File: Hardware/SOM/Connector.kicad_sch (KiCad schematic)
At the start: 1 part, among them J1 SODIMM-200_Split

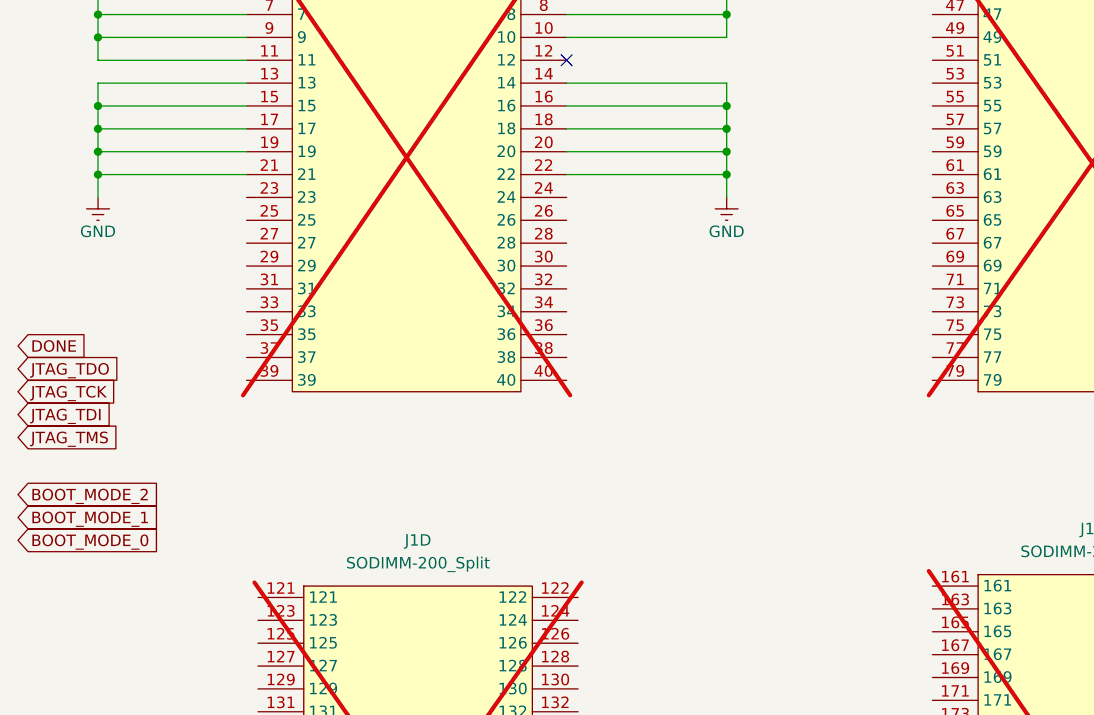
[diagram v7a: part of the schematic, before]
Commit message: SOM: layout update (QSPI+
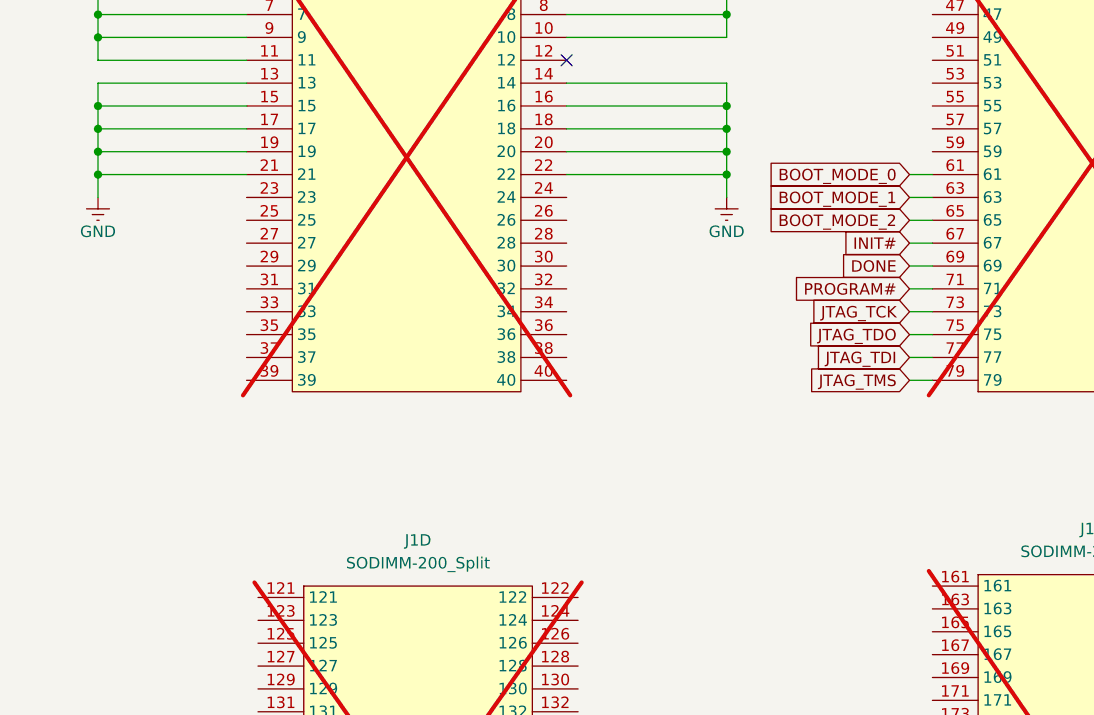
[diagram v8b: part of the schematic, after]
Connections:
- net BOOT_MODE_0: now also J1.61
- net BOOT_MODE_1: now also J1.63
- net BOOT_MODE_2: now also J1.65
- net DONE: now also J1.69
- net JTAG_TCK: now also J1.73
- net JTAG_TDI: now also J1.77
- net JTAG_TDO: now also J1.75
- net JTAG_TMS: now also J1.79
- net INIT#: now reaches J1.67
- net PROGRAM#: now reaches J1.71
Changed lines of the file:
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@@
+	(wire
+		(pts
+			(xy 119.38 68.58) (xy 121.92 68.58)
+		)
+		(stroke
+			(width 0)
+			(type default)
+		)
+	)
 	(wire
 		(pts
@@
 	(wire
 		(pts
+			(xy 119.38 78.74) (xy 121.92 78.74)
+		)
+		(stroke
+			(width 0)
+			(type default)
+		)
+	)
+	(wire
+		(pts
 			(xy 99.06 35.56) (xy 99.06 33.02)
 		)
@@
 	(wire
 		(pts
+			(xy 119.38 66.04) (xy 121.92 66.04)
+		)
+		(stroke
+			(width 0)
+			(type default)
+		)
+	)
+	(wire
+		(pts
 			(xy 99.06 50.8) (xy 99.06 53.34)
 		)
@@
 	(wire
 		(pts
+			(xy 119.38 63.5) (xy 121.92 63.5)
+		)
+		(stroke
+			(width 0)
+			(type default)
+		)
+	)
+	(wire
+		(pts
 			(xy 99.06 33.02) (xy 99.06 30.48)
 		)
@@
 	(wire
 		(pts
+			(xy 119.38 60.96) (xy 121.92 60.96)
+		)
+		(stroke
+			(width 0)
+			(type default)
+		)
+	)
+	(wire
+		(pts
 			(xy 99.06 38.1) (xy 99.06 35.56)
 		)
@@
 	(wire
 		(pts
+			(xy 119.38 73.66) (xy 121.92 73.66)
+		)
+		(stroke
+			(width 0)
+			(type default)
+		)
+	)
+	(wire
+		(pts
+			(xy 119.38 71.12) (xy 121.92 71.12)
+		)
+		(stroke
+			(width 0)
+			(type default)
+		)
+	)
+	(wire
+		(pts
 			(xy 29.21 40.64) (xy 29.21 38.1)
 		)
@@
 	(wire
 		(pts
+			(xy 119.38 76.2) (xy 121.92 76.2)
+		)
+		(stroke
+			(width 0)
+			(type default)
+		)
+	)
+	(wire
+		(pts
 			(xy 81.28 38.1) (xy 99.06 38.1)
 		)
@@
 	(wire
 		(pts
+			(xy 119.38 55.88) (xy 121.92 55.88)
+		)
+		(stroke
+			(width 0)
+			(type default)
+		)
+	)
+	(wire
+		(pts
 			(xy 29.21 48.26) (xy 45.72 48.26)
 		)
@@
 	(wire
 		(pts
+			(xy 119.38 58.42) (xy 121.92 58.42)
+		)
+		(stroke
+			(width 0)
+			(type default)
+		)
+	)
+	(wire
+		(pts
 			(xy 99.06 45.72) (xy 99.06 48.26)
 		)
@@
 	(global_label "JTAG_TDI"
 		(shape input)
-		(at 20.32 82.55 0)
-		(fields_autoplaced yes)
-		(effects
-			(font
-				(size 1.27 1.27)
-			)
-			(justify left)
-		)
-		(property "Intersheetrefs" "${INTERSHEET_REFS}"
-			(at 31.409 82.55 0)
-			(effects
-				(font
-					(size 1.27 1.27)
-				)
-				(justify left)
+		(at 119.38 76.2 180)
+		(fields_autoplaced yes)
+		(effects
+			(font
+				(size 1.27 1.27)
+			)
+			(justify right)
+		)
+		(property "Intersheetrefs" "${INTERSHEET_REFS}"
+			(at 108.291 76.2 0)
+			(effects
+				(font
+					(size 1.27 1.27)
+				)
+				(justify right)
+				(hide yes)
+			)
+		)
+	)
+	(global_label "PROGRAM#"
+		(shape input)
+		(at 119.38 68.58 180)
+		(fields_autoplaced yes)
+		(effects
+			(font
+				(size 1.27 1.27)
+			)
+			(justify right)
+		)
+		(property "Intersheetrefs" "${INTERSHEET_REFS}"
+			(at 106.1743 68.58 0)
+			(effects
+				(font
+					(size 1.27 1.27)
+				)
+				(justify right)
 				(hide yes)
 			)
@@
 	(global_label "BOOT_MODE_2"
 		(shape input)
-		(at 20.32 91.44 0)
-		(fields_autoplaced yes)
-		(effects
-			(font
-				(size 1.27 1.27)
-			)
-			(justify left)
-		)
-		(property "Intersheetrefs" "${INTERSHEET_REFS}"
-			(at 36.5494 91.44 0)
-			(effects
-				(font
-					(size 1.27 1.27)
-				)
-				(justify left)
+		(at 119.38 60.96 180)
+		(fields_autoplaced yes)
+		(effects
+			(font
+				(size 1.27 1.27)
+			)
+			(justify right)
+		)
+		(property "Intersheetrefs" "${INTERSHEET_REFS}"
+			(at 103.1506 60.96 0)
+			(effects
+				(font
+					(size 1.27 1.27)
+				)
+				(justify right)
 				(hide yes)
 			)
@@
 	(global_label "JTAG_TCK"
 		(shape input)
-		(at 20.32 80.01 0)
-		(fields_autoplaced yes)
-		(effects
-			(font
-				(size 1.27 1.27)
-			)
-			(justify left)
-		)
-		(property "Intersheetrefs" "${INTERSHEET_REFS}"
-			(at 32.0742 80.01 0)
-			(effects
-				(font
-					(size 1.27 1.27)
-				)
-				(justify left)
+		(at 119.38 71.12 180)
+		(fields_autoplaced yes)
+		(effects
+			(font
+				(size 1.27 1.27)
+			)
+			(justify right)
+		)
+		(property "Intersheetrefs" "${INTERSHEET_REFS}"
+			(at 107.6258 71.12 0)
+			(effects
+				(font
+					(size 1.27 1.27)
+				)
+				(justify right)
 				(hide yes)
 			)
@@
 	(global_label "BOOT_MODE_1"
 		(shape input)
-		(at 20.32 93.98 0)
-		(fields_autoplaced yes)
-		(effects
-			(font
-				(size 1.27 1.27)
-			)
-			(justify left)
-		)
-		(property "Intersheetrefs" "${INTERSHEET_REFS}"
-			(at 36.5494 93.98 0)
-			(effects
-				(font
-					(size 1.27 1.27)
-				)
-				(justify left)
+		(at 119.38 58.42 180)
+		(fields_autoplaced yes)
+		(effects
+			(font
+				(size 1.27 1.27)
+			)
+			(justify right)
+		)
+		(property "Intersheetrefs" "${INTERSHEET_REFS}"
+			(at 103.1506 58.42 0)
+			(effects
+				(font
+					(size 1.27 1.27)
+				)
+				(justify right)
 				(hide yes)
 			)
@@
 	(global_label "JTAG_TDO"
 		(shape input)
-		(at 20.32 77.47 0)
-		(fields_autoplaced yes)
-		(effects
-			(font
-				(size 1.27 1.27)
-			)
-			(justify left)
-		)
-		(property "Intersheetrefs" "${INTERSHEET_REFS}"
-			(at 32.1347 77.47 0)
-			(effects
-				(font
-					(size 1.27 1.27)
-				)
-				(justify left)
+		(at 119.38 73.66 180)
+		(fields_autoplaced yes)
+		(effects
+			(font
+				(size 1.27 1.27)
+			)
+			(justify right)
+		)
+		(property "Intersheetrefs" "${INTERSHEET_REFS}"
+			(at 107.5653 73.66 0)
+			(effects
+				(font
+					(size 1.27 1.27)
+				)
+				(justify right)
+				(hide yes)
+			)
+		)
+	)
+	(global_label "INIT#"
+		(shape input)
+		(at 119.38 63.5 180)
+		(fields_autoplaced yes)
+		(effects
+			(font
+				(size 1.27 1.27)
+			)
+			(justify right)
+		)
+		(property "Intersheetrefs" "${INTERSHEET_REFS}"
+			(at 111.6171 63.5 0)
+			(effects
+				(font
+					(size 1.27 1.27)
+				)
+				(justify right)
 				(hide yes)
 			)
@@
 	(global_label "BOOT_MODE_0"
 		(shape input)
-		(at 20.32 96.52 0)
-		(fields_autoplaced yes)
-		(effects
-			(font
-				(size 1.27 1.27)
-			)
-			(justify left)
-		)
-		(property "Intersheetrefs" "${INTERSHEET_REFS}"
-			(at 36.5494 96.52 0)
-			(effects
-				(font
-					(size 1.27 1.27)
-				)
-				(justify left)
+		(at 119.38 55.88 180)
+		(fields_autoplaced yes)
+		(effects
+			(font
+				(size 1.27 1.27)
+			)
+			(justify right)
+		)
+		(property "Intersheetrefs" "${INTERSHEET_REFS}"
+			(at 103.1506 55.88 0)
+			(effects
+				(font
+					(size 1.27 1.27)
+				)
+				(justify right)
 				(hide yes)
 			)
@@
 	(global_label "DONE"
 		(shape input)
-		(at 20.32 74.93 0)
-		(fields_autoplaced yes)
-		(effects
-			(font
-				(size 1.27 1.27)
-			)
-			(justify left)
-		)
-		(property "Intersheetrefs" "${INTERSHEET_REFS}"
-			(at 28.3852 74.93 0)
-			(effects
-				(font
-					(size 1.27 1.27)
-				)
-				(justify left)
+		(at 119.38 66.04 180)
+		(fields_autoplaced yes)
+		(effects
+			(font
+				(size 1.27 1.27)
+			)
+			(justify right)
+		)
+		(property "Intersheetrefs" "${INTERSHEET_REFS}"
+			(at 111.3148 66.04 0)
+			(effects
+				(font
+					(size 1.27 1.27)
+				)
+				(justify right)
 				(hide yes)
 			)
@@
 	(global_label "JTAG_TMS"
 		(shape input)
-		(at 20.32 85.09 0)
-		(fields_autoplaced yes)
-		(effects
-			(font
-				(size 1.27 1.27)
-			)
-			(justify left)
-		)
-		(property "Intersheetrefs" "${INTERSHEET_REFS}"
-			(at 32.1951 85.09 0)
-			(effects
-				(font
-					(size 1.27 1.27)
-				)
-				(justify left)
-				(hide yes)
-			)
+		(at 119.38 78.74 180)
+		(fields_autoplaced yes)
+		(effects
+			(font
+				(size 1.27 1.27)
+			)
+			(justify right)
+		)
+		(property "Intersheetrefs" "${INTERSHEET_REFS}"
+			(at 107.5049 78.74 0)
+			(effects
+				(font
+					(size 1.27 1.27)
+				)
+				(justify right)
+				(hide yes)
+			)
